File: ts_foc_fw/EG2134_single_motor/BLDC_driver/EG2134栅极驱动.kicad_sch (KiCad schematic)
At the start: 1 part, among them U1 EG2134_N

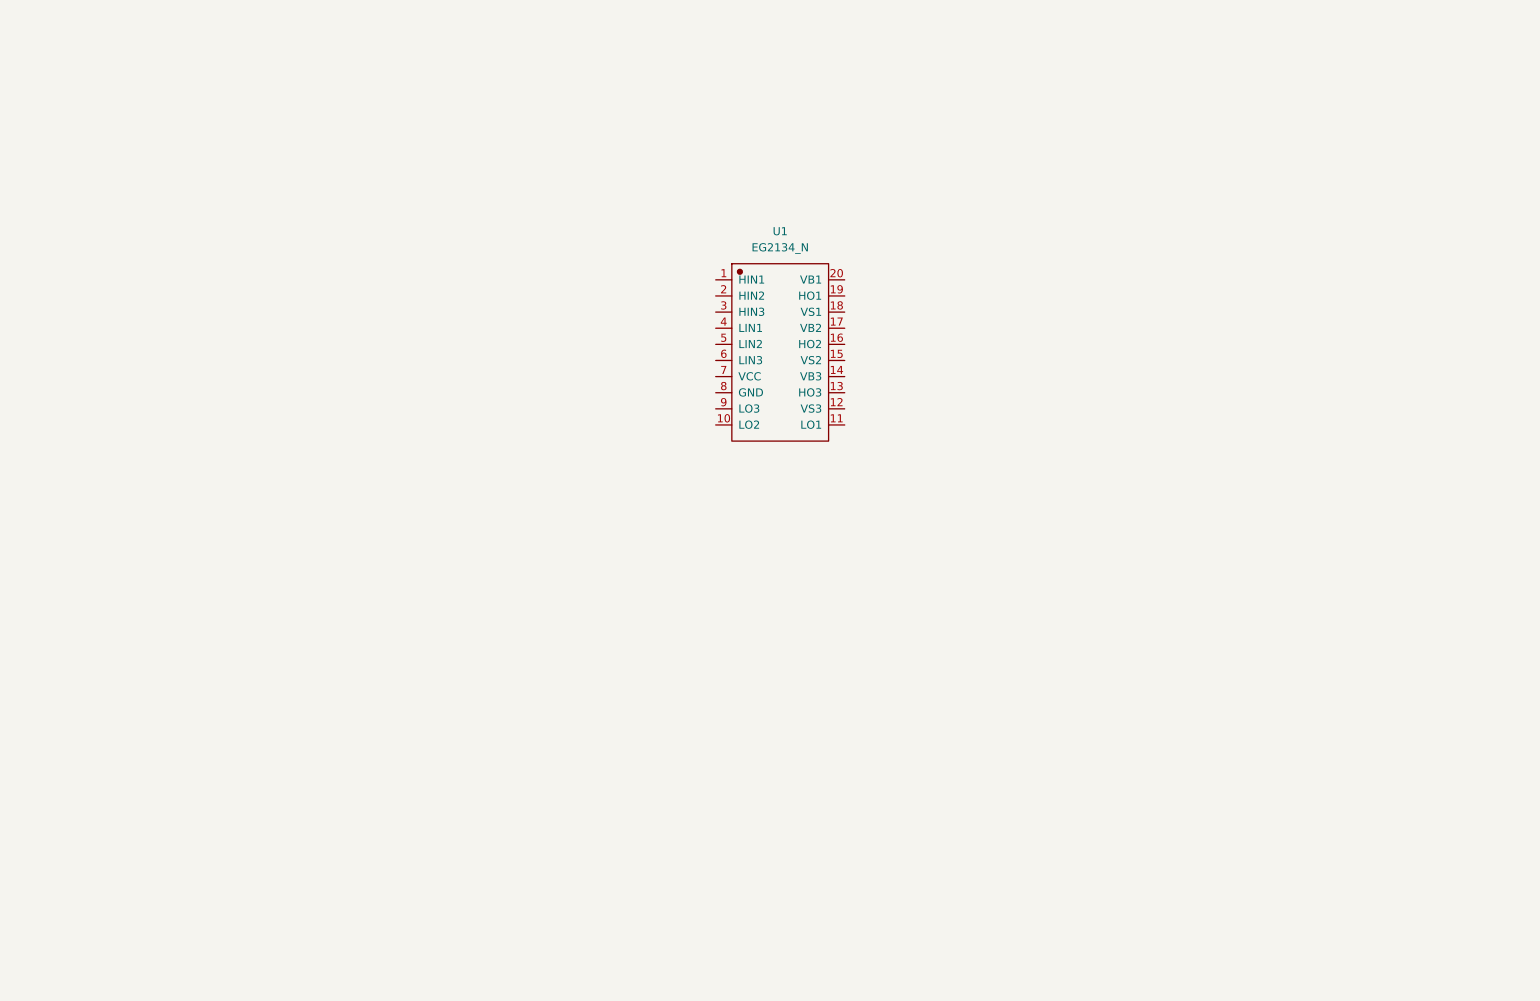
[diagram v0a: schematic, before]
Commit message: 原理图移植完成,PCB还没有布局
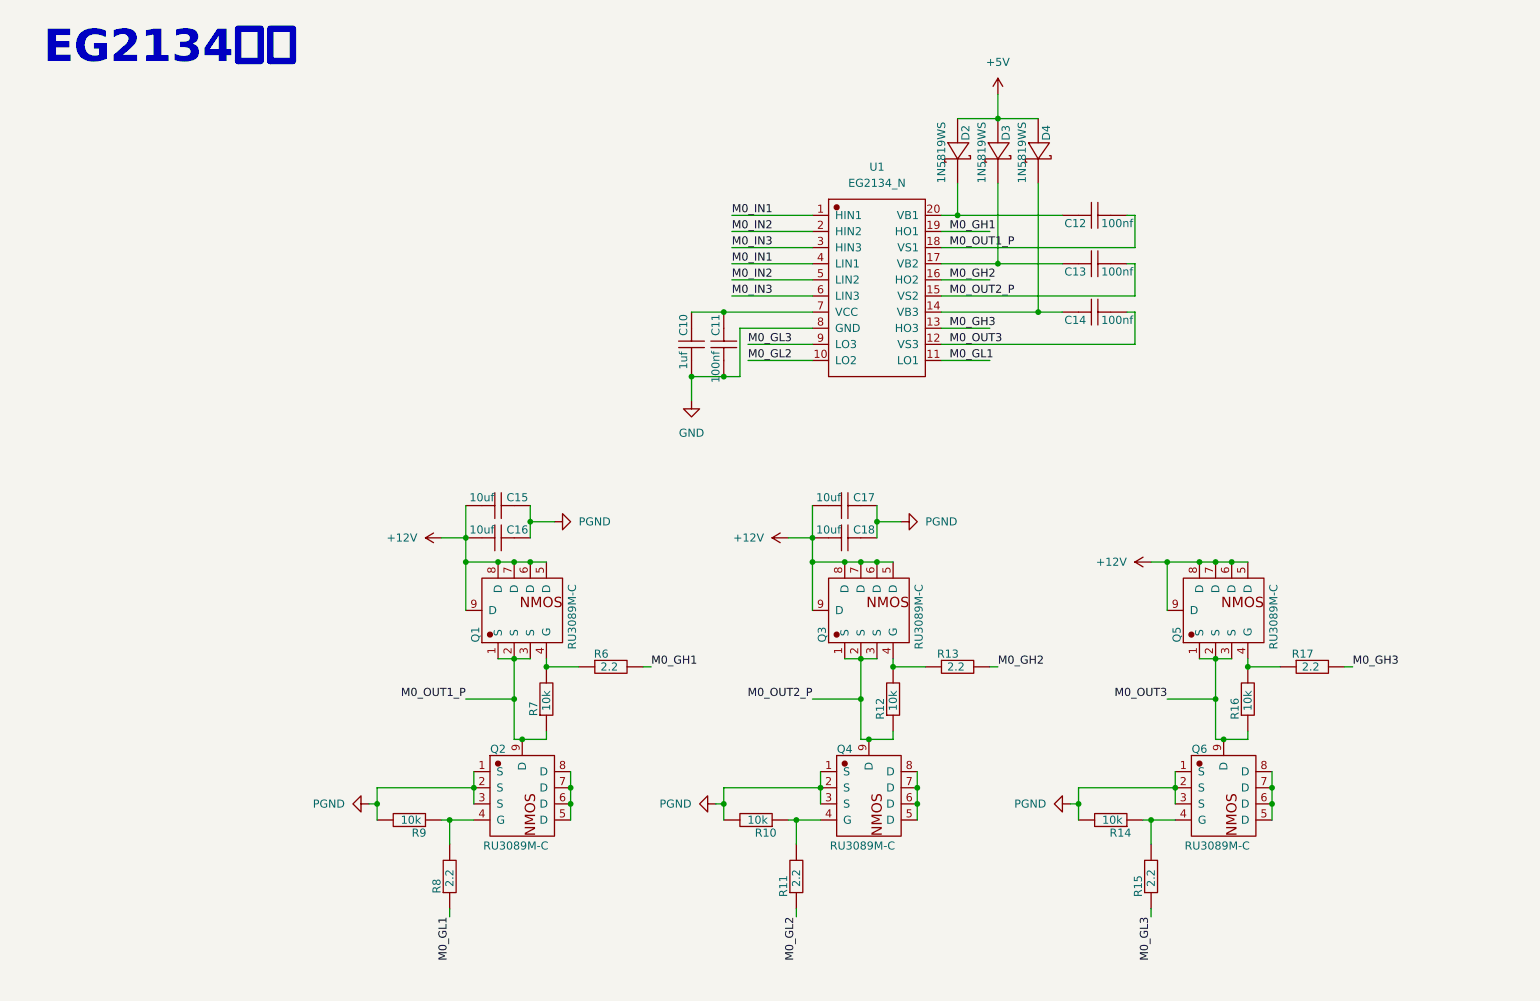
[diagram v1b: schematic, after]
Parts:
- added C10: 1uf, BLDC_Drive_Tsfoc:C0603, symbol BLDC_Drive_Tsfoc:cap
- added C11, C12, C13, C14: 100nf, BLDC_Drive_Tsfoc:C0603, symbol BLDC_Drive_Tsfoc:cap
- added C15, C16, C17, C18: 10uf, BLDC_Drive_Tsfoc:C0805, symbol BLDC_Drive_Tsfoc:cap
- added D2, D3, D4: 1N5819WS, BLDC_Drive_Tsfoc:1N5819WS, symbol BLDC_Drive_Tsfoc:1N5819WS
- added Q1, Q2, Q3, Q4, Q5, Q6: RU3089M-C, BLDC_Drive_Tsfoc:RU3089M-C, symbol BLDC_Drive_Tsfoc:RU3089M-C
- added R10, R12, R14, R16, R7, R9: 10k, BLDC_Drive_Tsfoc:R0402, symbol BLDC_Drive_Tsfoc:res
- added R11, R13, R15, R17, R6, R8: 2.2, BLDC_Drive_Tsfoc:R0402, symbol BLDC_Drive_Tsfoc:res
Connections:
- net M0_IN1: now reaches U1.1 (HIN1)
- net M0_IN1: now also U1.4 (LIN1)
- net M0_GL2: now reaches U1.10 (LO2)
- net M0_GL2: now also R11.1
- net M0_GL1: now reaches U1.11 (LO1)
- net M0_GL1: now also R8.1
- net M0_OUT3: now reaches U1.12 (VS3)
- net M0_OUT3: now also C14.1, Q5.1 (S), Q5.2 (S), Q5.3 (S), Q6.9 (D), R16.1
- net M0_GH3: now reaches U1.13 (HO3)
- net M0_GH3: now also R17.2
- net at U1.14 (VB3): now also C14.2, D4.1 (K)
- net M0_OUT2_P: now reaches U1.15 (VS2)
- net M0_OUT2_P: now also C13.1, Q3.1 (S), Q3.2 (S), Q3.3 (S), Q4.9 (D), R12.1
- net M0_GH2: now reaches U1.16 (HO2)
- net M0_GH2: now also R13.2
- net at U1.17 (VB2): now also C13.2, D3.1 (K)
- net M0_OUT1_P: now reaches U1.18 (VS1)
- net M0_OUT1_P: now also C12.1, Q1.1 (S), Q1.2 (S), Q1.3 (S), Q2.9 (D), R7.1
- net M0_GH1: now reaches U1.19 (HO1)
- net M0_GH1: now also R6.2
- net M0_IN2: now reaches U1.2 (HIN2)
- net M0_IN2: now also U1.5 (LIN2)
- net at U1.20 (VB1): now also C12.2, D2.1 (K)
- net M0_IN3: now reaches U1.3 (HIN3)
- net M0_IN3: now also U1.6 (LIN3)
- net at U1.7 (VCC): now also C10.2, C11.2
- net GND: now reaches U1.8 (GND)
- net GND: now also C10.1, C11.1
- net M0_GL3: now reaches U1.9 (LO3)
- net M0_GL3: now also R15.1
- new net: Q4.4 (G), R10.1, R11.2
- new net: Q4.5 (D), Q4.6 (D), Q4.7 (D), Q4.8 (D)
- new net: Q2.4 (G), R8.2, R9.1
- new net: Q6.4 (G), R14.1, R15.2
- new net: Q6.5 (D), Q6.6 (D), Q6.7 (D), Q6.8 (D)
- new net: Q1.4 (G), R6.1, R7.2
- new net: Q5.4 (G), R16.2, R17.1
- new net: Q3.4 (G), R12.2, R13.1
- new net: Q2.5 (D), Q2.6 (D), Q2.7 (D), Q2.8 (D)
- new net +12V: C15.1, C16.1, C17.1, C18.1, Q1.5 (D), Q1.6 (D), Q1.7 (D), Q1.8 (D), Q1.9 (D), Q3.5 (D), Q3.6 (D), Q3.7 (D), Q3.8 (D), Q3.9 (D), Q5.5 (D), Q5.6 (D), Q5.7 (D), Q5.8 (D), Q5.9 (D)
- new net +5V: D2.2 (A), D3.2 (A), D4.2 (A)
- new net PGND: C15.2, C16.2, C17.2, C18.2, Q2.1 (S), Q2.2 (S), Q2.3 (S), Q4.1 (S), Q4.2 (S), Q4.3 (S), Q6.1 (S), Q6.2 (S), Q6.3 (S), R10.2, R14.2, R9.2
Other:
- note added: "EG2134驱动"
- moved on the sheet: U1

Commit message: dayly
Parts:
- U1: footprint BLDC_Drive_Tsfoc:EG2134_N_TSSOP-20_L6.5-W4.4-P0.65-LS6.4-BL -> BLDC_Drive_Tsfoc:EG2134
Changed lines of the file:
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@@
 			)
 		)
-		(property "Footprint" "BLDC_Drive_Tsfoc:EG2134_N_TSSOP-20_L6.5-W4.4-P0.65-LS6.4-BL"
+		(property "Footprint" "BLDC_Drive_Tsfoc:EG2134"
 			(at 150.368 58.928 0)
 			(effects

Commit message: PCB_layout_ing
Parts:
- added R20: 0, BLDC_Drive_Tsfoc:R0805, symbol BLDC_Drive_Tsfoc:res
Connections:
- net GND: now also R20.1
- net M0_OUT1_P: now also Q2.5 (D), Q2.6 (D), Q2.7 (D), Q2.8 (D)
- net M0_OUT2_P: now also Q4.5 (D), Q4.6 (D), Q4.7 (D), Q4.8 (D)
- net M0_OUT3: now also Q6.5 (D), Q6.6 (D), Q6.7 (D), Q6.8 (D)
- net PGND: now also R20.2
